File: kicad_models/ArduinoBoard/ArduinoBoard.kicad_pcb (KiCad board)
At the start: 2 copper layers, 70 x 52 mm, 9 parts, among them J1 5V Output, J11 Conn_02x04_Odd_Even, J14 Switch/Buttons, J2 5V Output, J3 PWM Output, J4 12V Input, J5 Conn_01x04_Pin, J7 Conn_01x06_Pin

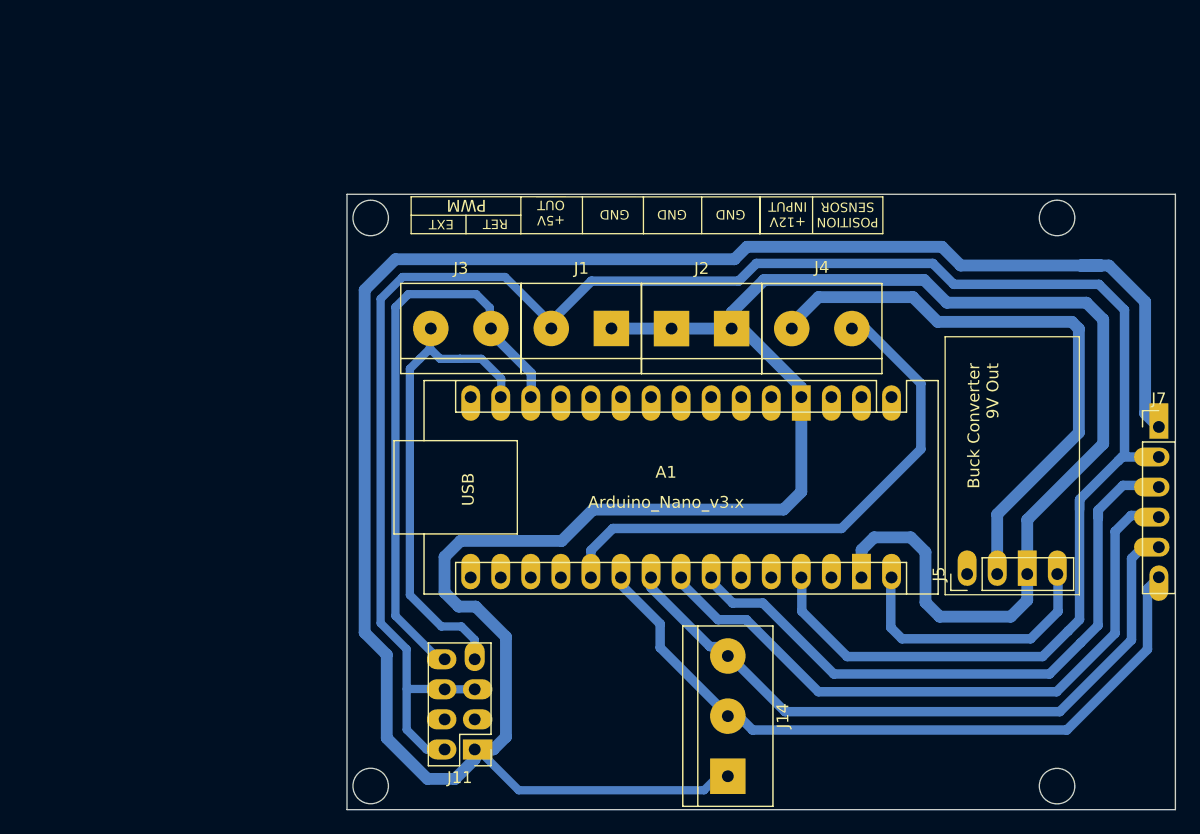
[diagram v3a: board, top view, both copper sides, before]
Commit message: Updated a couple of measurements on the user.1 layer.
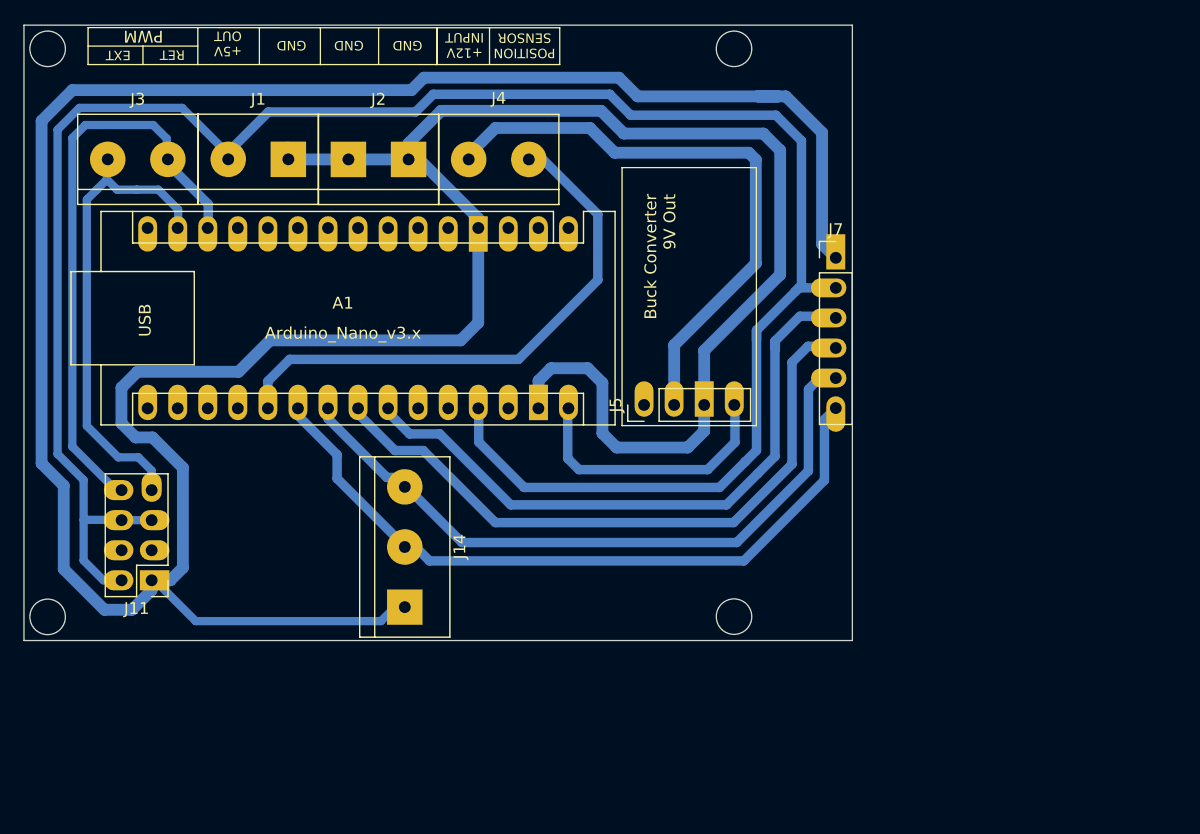
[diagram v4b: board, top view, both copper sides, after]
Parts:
- moved J1 30.8 mm to (123.7, 84.8)
- moved J11 30.8 mm to (117.2, 120.4)
- moved A1 30.8 mm to (152.4, 90.6)
- moved J14 30.8 mm to (138.6, 112.5)
- moved J2 30.8 mm to (133.8, 84.8)
- moved J3 30.8 mm to (113.5, 84.8)
- moved J4 30.8 mm to (144.0, 84.8)
- moved J5 30.8 mm to (158.8, 105.6)
- moved J7 30.8 mm to (175.0, 93.2)
